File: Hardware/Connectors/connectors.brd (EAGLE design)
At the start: 104.3 x 90 mm, 14 parts, among them X1 KUSBVX, X2 KUSBVX, X3 5566-2

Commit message: Added lates MPPT Tracking PCB design
Also cleaned hardware folder, removing non-working current sense
designs.
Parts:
- moved X1 4.47 mm to (24.8, 28.6), turned to 180 degrees
- moved X2 2.66 mm to (45.1, 28.6), turned to 180 degrees
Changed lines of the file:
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@@
 <element name="U$3" library="equinox" package="KYCON_KLVDX_2020_B" value="KYCON_KLDVX-0202" x="32.71" y="9.37" rot="MR0"/>
 <element name="U$4" library="equinox" package="KYCON_KLVDX_2020_B" value="KYCON_KLDVX-0202" x="13.47" y="9.37" rot="MR0"/>
-<element name="X1" library="con-kycon" package="KUSBVX" value="KUSBVX" x="21.01" y="26.23" rot="MR0"/>
-<element name="X2" library="con-kycon" package="KUSBVX" value="KUSBVX" x="46.23" y="26.23" rot="MR0"/>
+<element name="X1" library="con-kycon" package="KUSBVX" value="KUSBVX" x="24.7735" y="28.634" rot="MR180"/>
+<element name="X2" library="con-kycon" package="KUSBVX" value="KUSBVX" x="45.083" y="28.634" rot="MR180"/>
 <element name="X3" library="con-molex" package="5566-2" value="5566-2" x="6.84" y="74.34" rot="R180">
 <attribute name="OC_NEWARK" value="unknown" x="-12.21" y="139.11" size="1.778" layer="27" rot="R180" display="off"/>

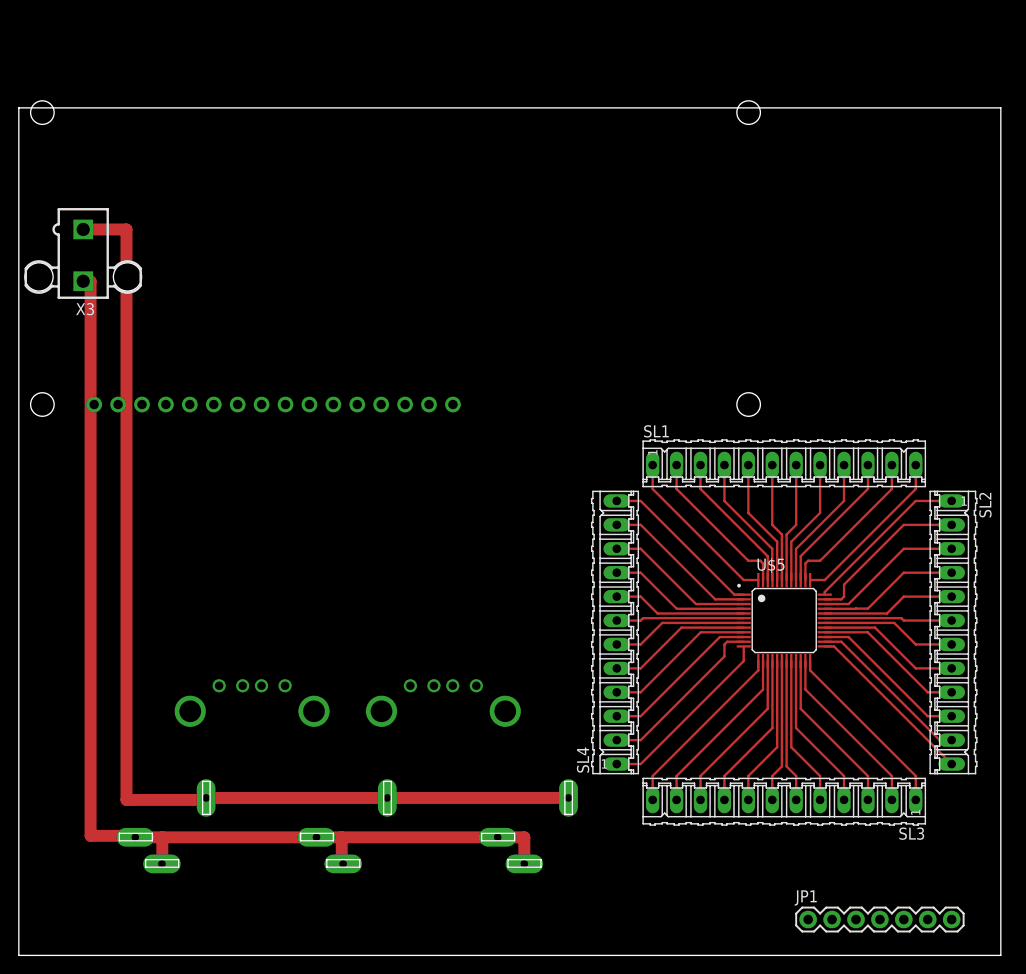
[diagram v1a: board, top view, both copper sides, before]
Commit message: First Version of Standalone Connectors Layout
Prototype Faceplate is being designed based on this layout.
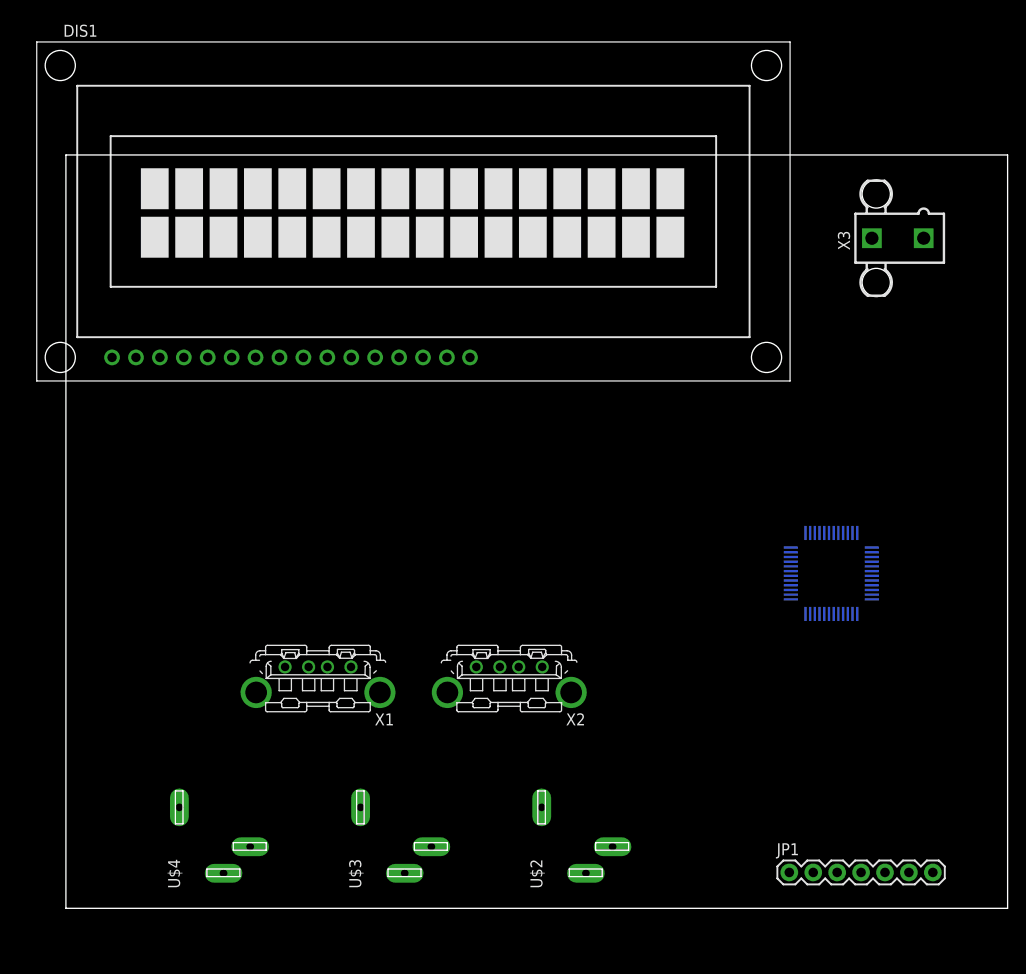
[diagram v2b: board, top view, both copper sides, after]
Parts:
- removed SL1, SL2, SL3, SL4: (no value), con-amp-quick:12P
- DIS1: value TUXGR_16X2_R2 -> LCD_16X2_R2; device display-lcd:TUXGR_16X2_R2 -> equinox:LCD_16X2_R2
- moved X3 86.5 mm to (93.3, 76.2), turned to 90 degrees
- moved U$1 53.1 mm to (87.3, 19.9)
- moved DIS1 40.3 mm to (1.90, 61.0), flipped to the top, turned to 0 degrees
- moved U$2 10.0 mm to (62.0, 8.37), flipped to the top
- moved U$3 10.0 mm to (42.7, 8.37), flipped to the top
- moved U$4 10.0 mm to (23.5, 8.37), flipped to the top
- moved X1 7.28 mm to (31.8, 30.6), flipped to the top
- moved X2 7.28 mm to (52.1, 30.6), flipped to the top
- moved U$5 7.07 mm to (86.3, 40.6), flipped to the bottom
- moved JP1 5.39 mm to (81.8, 8.81)
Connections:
- removed net N$10: SL1.8, U$5.41
- removed net N$11: SL1.9, U$5.40
- removed net N$12: SL1.10, U$5.39
- removed net N$13: SL1.11, U$5.38
- removed net N$14: SL1.12, U$5.37
- removed net N$15: SL4.12, U$5.1
- removed net N$16: SL4.11, U$5.2
- removed net N$17: SL4.9, U$5.4
- removed net N$18: SL4.10, U$5.3
- removed net N$19: SL4.8, U$5.5
- removed net N$20: SL4.7, U$5.6
- removed net N$21: SL4.6, U$5.7
- removed net N$22: SL4.4, U$5.9
- removed net N$23: SL4.5, U$5.8
- removed net N$24: SL4.3, U$5.10
- removed net N$25: SL4.2, U$5.11
- removed net N$26: SL4.1, U$5.12
- removed net N$27: SL3.12, U$5.13
- removed net N$28: SL3.11, U$5.14
- removed net N$29: SL3.10, U$5.15
- removed net N$3: SL1.1, U$5.48
- removed net N$30: SL3.9, U$5.16
- removed net N$31: SL3.8, U$5.17
- removed net N$32: SL3.7, U$5.18
- removed net N$33: SL3.6, U$5.19
- removed net N$34: SL3.5, U$5.20
- removed net N$35: SL3.4, U$5.21
- removed net N$36: SL3.3, U$5.22
- removed net N$37: SL3.2, U$5.23
- removed net N$38: SL3.1, U$5.24
- removed net N$39: SL2.1, U$5.36
- removed net N$4: SL1.2, U$5.47
- removed net N$40: SL2.2, U$5.35
- removed net N$41: SL2.3, U$5.34
- removed net N$42: SL2.4, U$5.33
- removed net N$43: SL2.5, U$5.32
- removed net N$44: SL2.6, U$5.31
- removed net N$45: SL2.7, U$5.30
- removed net N$46: SL2.8, U$5.29
- removed net N$47: SL2.9, U$5.28
- removed net N$48: SL2.10, U$5.27
- removed net N$49: SL2.11, U$5.26
- removed net N$5: SL1.3, U$5.46
- removed net N$50: SL2.12, U$5.25
- removed net N$6: SL1.4, U$5.45
- removed net N$7: SL1.5, U$5.44
- removed net N$8: SL1.6, U$5.43
- removed net N$9: SL1.7, U$5.42
- new net VDD: U$5.24
- new net VDD_: U$5.48
- new net VSS: U$5.23
- new net VSS_: U$5.47
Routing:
- net N$2: track 114.5 -> 0.00 mm
- net N$1: track 112.3 -> 0.00 mm
- net N$26: track 19.6 -> 0.00 mm
- net N$38: track 19.4 -> 0.00 mm
- net N$27: track 19.4 -> 0.00 mm
- net N$49: track 19.1 -> 0.00 mm
- net N$50: track 18.7 -> 0.00 mm
- net N$25: track 18.6 -> 0.00 mm
- net N$28: track 18.6 -> 0.00 mm
- net N$37: track 18.6 -> 0.00 mm
- net N$39: track 17.8 -> 0.00 mm
- net N$3: track 17.8 -> 0.00 mm
- net N$14: track 17.8 -> 0.00 mm
- net N$36: track 17.7 -> 0.00 mm
- net N$29: track 17.7 -> 0.00 mm
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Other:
- board size 104.3 x 90 mm -> 100 x 80 mm
- board text added: "INNER BOX DIMENSIONS"
- board text added: "KEYPAD"
- board text added: "OUTER BOX DIMENSIONS"
